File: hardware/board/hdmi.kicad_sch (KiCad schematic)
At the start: 1 part, among them U1 RK3568

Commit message: emmc stuff
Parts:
- U1: LCSC (none) -> C3345225
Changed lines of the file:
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@@
+			)
+		)
+		(property "LCSC" "C3345225"
+			(at 27.94 78.74 0)
+			(effects
+				(font
+					(size 1.27 1.27)
+				)
+				(hide yes)
 			)
 		)

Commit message: start of ethernet
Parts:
- added C147: 1uF X5R 10V, Capacitor_SMD:C_0402_1005Metric, symbol Device:C
- added D12, D13: ESD5344D, lcsc:DFN2510-10_L2.5-W1.0-P0.50-BL, symbol lcsc:ESD5344D
- added D14, D15: B5819WS_C916992, lcsc:SOD-323_L1.7-W1.3-LS2.5-RD, symbol lcsc:B5819WS_C916992
- added J1: HDMI_A, Connector_Video:HDMI_A_Amphenol_10029449-x01xLF_Horizontal, symbol Connector:HDMI_A
- added Q6, Q7, Q8: 2SK3018_C194460, lcsc:SOT-323-3_L2.0-W1.3-P1.30-LS2.1-BR, symbol lcsc:2SK3018_C194460
- added R82, R85: 1.8K 5%, Resistor_SMD:R_0402_1005Metric, symbol Device:R
- added R83, R84: 10K 5%, Resistor_SMD:R_0402_1005Metric, symbol Device:R
- added R86: 27K 5%, Resistor_SMD:R_0402_1005Metric, symbol Device:R
- added R87: 1K 5%, Resistor_SMD:R_0402_1005Metric, symbol Device:R
- added R88: 100K 5%, Resistor_SMD:R_0402_1005Metric, symbol Device:R
- added unit 13 of U1
- added U28, U29, U30, U31: ESD5341N, lcsc:DFN1006-2L-RD, symbol lcsc:ESD5341N
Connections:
- new net: D13.1, J1.12 (CK-)
- new net: D13.2, J1.10 (CK+)
- new net: D13.4, J1.9 (D0-)
- new net: D13.5, J1.7 (D0+)
- new net: D12.1, J1.1 (D2+)
- new net: D12.2, J1.3 (D2-)
- new net: D12.4, J1.4 (D1+)
- new net: D12.5, J1.6 (D1-)
- new net: Q7.1 (G), R85.2
- new net: D15.1 (K), R82.1, R85.1
- new net: Q6.1 (G), R82.2
- new net GND: C147.2, D12.3, D12.8, D13.3, D13.8, J1.11 (CKS), J1.17 (GND), J1.2 (D2S), J1.5 (D1S), J1.8 (D0S), J1.SH, R88.2, U28.2, U29.2, U30.2, U31.2
- new net HDMITX_CEC_M0: Q8.2 (S), R86.2
- new net HDMITX_SCL: Q6.2 (S), R83.2
- new net HDMITX_SDA: Q7.2 (S), R84.2
- new net HDMI_TX0N_PORT: D13.7
- new net HDMI_TX0P_PORT: D13.6
- new net HDMI_TX1N_PORT: D12.6
- new net HDMI_TX1P_PORT: D12.7
- new net HDMI_TX2N_PORT: D12.9
- new net HDMI_TX2P_PORT: D12.10
- new net HDMI_TXCLKN_PORT: D13.10
- new net HDMI_TXCLKP_PORT: D13.9
- new net HDMI_TXDDC_SCL_PORT: J1.15 (SCL), Q6.3 (D), U30.1
- new net HDMI_TXDDC_SDA_PORT: J1.16 (SDA), Q7.3 (D), U29.1
- new net HDMI_TX_CEC_PORT: J1.13 (CEC), Q8.3 (D), U31.1
- new net HDMI_TX_HPDIN: R87.1
- new net HDMI_TX_HPD_PORT: J1.19 (HPD), R87.2, R88.1, U28.1
- new net VCC_3V3: R83.1, R84.1, R86.1
- new net VCC_5V0: D14.2 (A), D15.2 (A), Q8.1 (G)
- new net VCC_5V0_HDMI_TX: C147.1, D14.1 (K), J1.18 (+5V)
- no-connect marks 0 -> 1
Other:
- moved on the sheet: U1P

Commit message: finished schematic!
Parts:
- added C352, C364, C365, C367: 100nF X5R 10V, Capacitor_SMD:C_0201_0603Metric, symbol Device:C
- added C366, C368: 4.7uF X5R 6.3V, Capacitor_SMD:C_0402_1005Metric, symbol Device:C
- added L12: L_Iron_Coupled_Small, lcsc:FILTER-SMD_4P-L2.0-W1.2-BL_DLW21H, symbol Device:L_Iron_Coupled_Small
- added R209, R210, R211, R212, R213, R214, R215, R216: 2.2R 5%, Resistor_SMD:R_0402_1005Metric, symbol Device:R
- added R217: 1.62K 1%, Resistor_SMD:R_0201_0603Metric, symbol Device:R
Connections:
- net GND: now also C352.2, C364.2, C365.2, C366.2, C367.2, C368.2, R217.1
- net HDMITX_CEC_M0: now also U1.AH6 (GPIO4_D1_U)
- net HDMITX_SCL: now also U1.AG8 (GPIO4_C7_U)
- net HDMITX_SDA: now also U1.AG7 (GPIO4_D0_U)
- net HDMI_TX0N_PORT: now also R210.1
- net HDMI_TX0P_PORT: now also R209.1
- net HDMI_TX1N_PORT: now also R212.1
- net HDMI_TX1P_PORT: now also R211.1
- net HDMI_TX2N_PORT: now also R214.1
- net HDMI_TX2P_PORT: now also R213.1
- net HDMI_TXCLKN_PORT: now also L12.3, R216.1
- net HDMI_TXCLKP_PORT: now also L12.1, R215.1
- net HDMI_TX_AVDD_0V9: now also C365.1, C366.1
- net HDMI_TX_HPDIN: now also U1.AB18 (HDMI_TX_HPDIN), C364.1
- net VCC_3V3: now also U1.V12 (VCCIO7), C352.1
- net PCIE30X2_WAKEn_M2: now reaches U1.AA11 (GPIO4_C3_D)
- net TYPEC_SW_SEL_GPIO4_D2: now reaches U1.AB9 (GPIO4_D2_D)
- net PCIE30X2_CLKREQn_M2: now reaches U1.AF8 (GPIO4_C2_D)
- net PCIE30X2_PERSTn_M2: now reaches U1.AH7 (GPIO4_C4_D)
- net at U1.AA18 (HDMI_TX_REXT): now also R217.2
- net at U1.AG19 (HDMI_TX_CLKN): now also L12.4, R216.2
- net at U1.AG20 (HDMI_TX_D0P): now also R209.2
- net at U1.AG21 (HDMI_TX_D1P): now also R211.2
- net at U1.AG22 (HDMI_TX_D2P): now also R213.2
- net at U1.AH19 (HDMI_TX_CLKP): now also L12.2, R215.2
- net at U1.AH20 (HDMI_TX_D0N): now also R210.2
- net at U1.AH21 (HDMI_TX_D1N): now also R212.2
- net at U1.AH22 (HDMI_TX_D2N): now also R214.2
- net VCCA1V8_IMAGE: now reaches U1.W18 (HDMI_TX_AVDD_1V8)
- net VCCA1V8_IMAGE: now also C367.1, C368.1
- no-connect marks 1 -> 3
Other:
- note added: "Diff 100 Ohm ±10%"
- note added: "HDMI"
- moved on the sheet: C147, D12, D13, D15, J1, Q6, Q7, R82, R83, R84, R85, U1M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

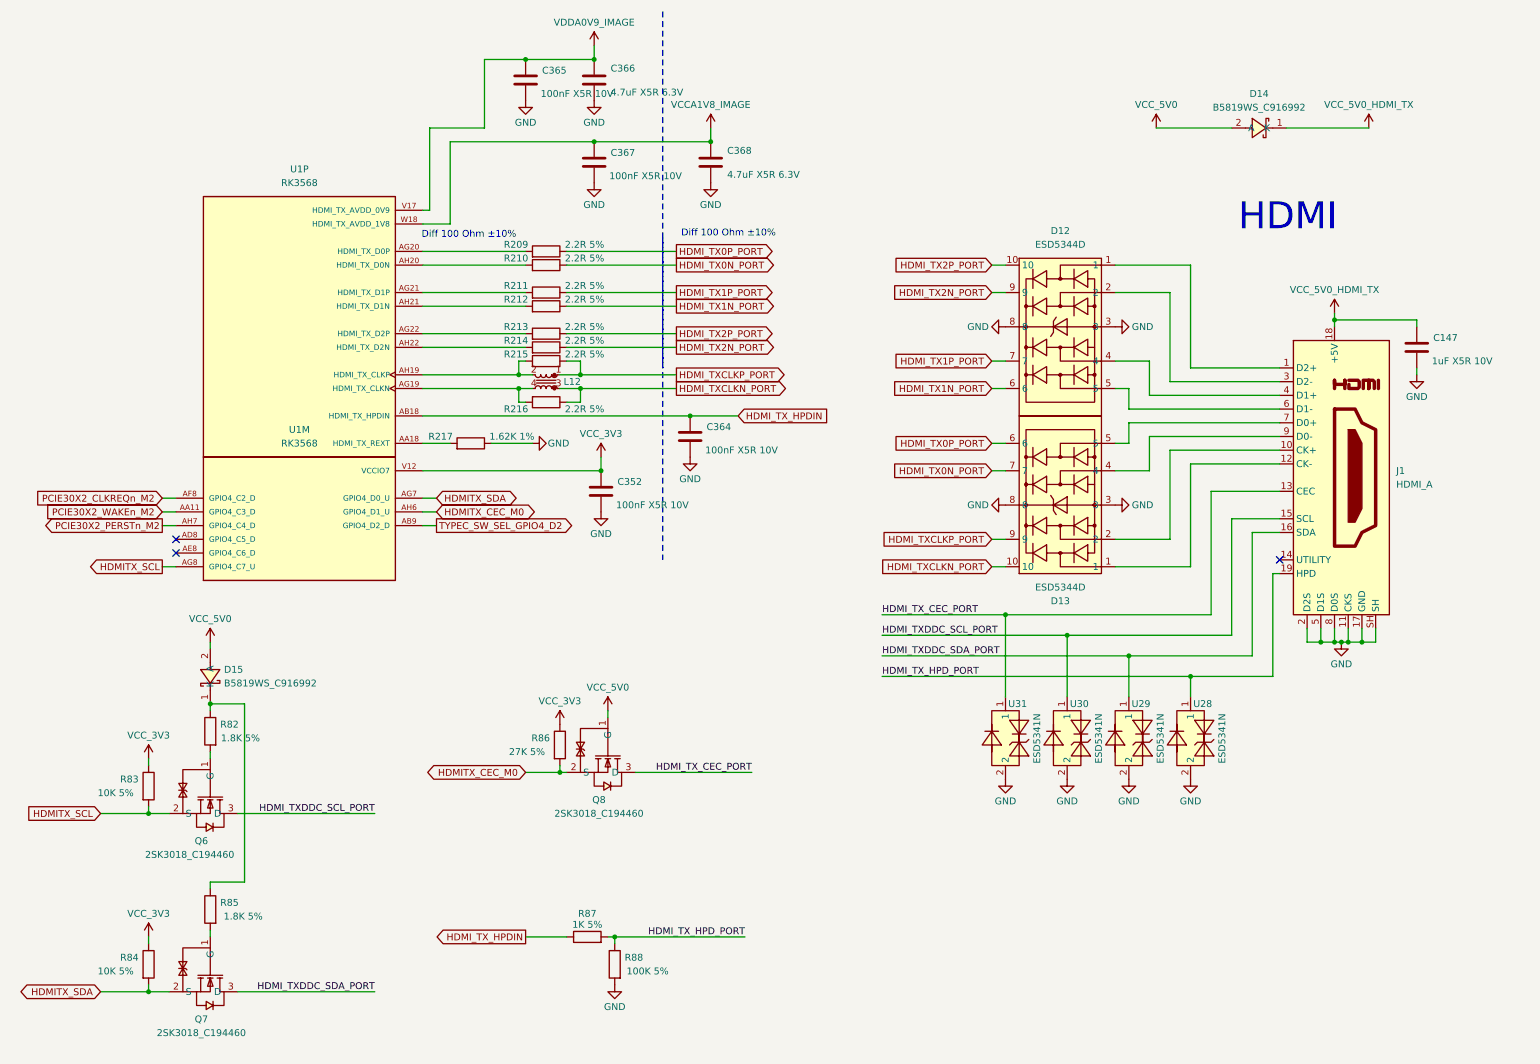
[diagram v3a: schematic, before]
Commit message: finished beautifying schematic
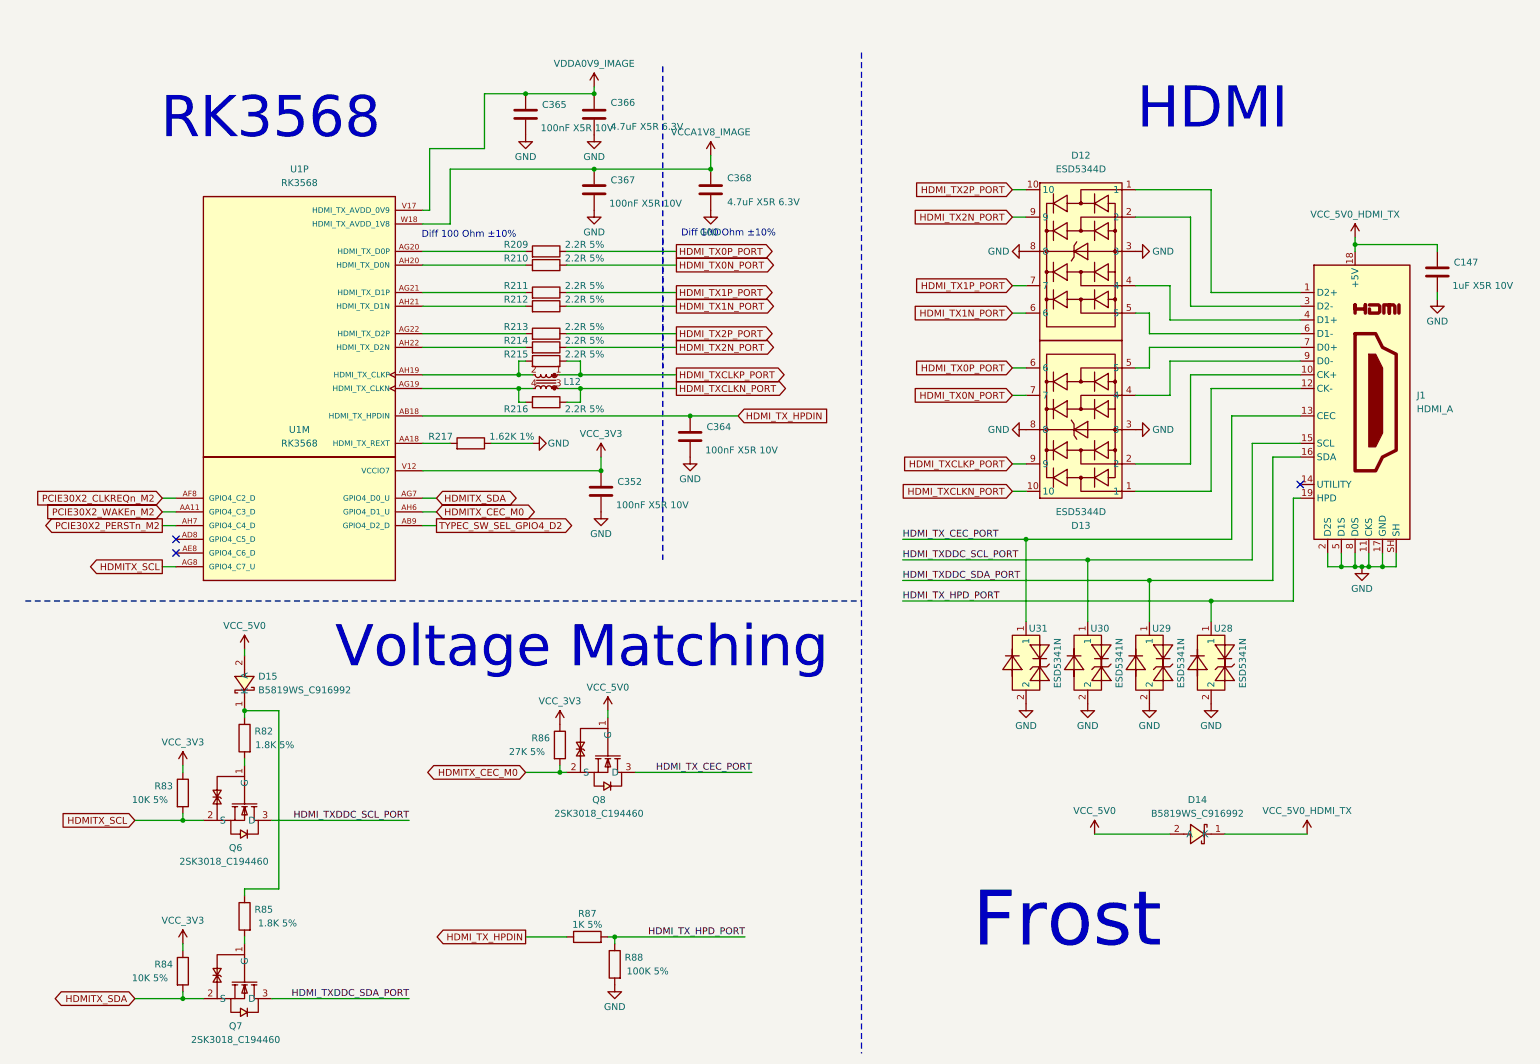
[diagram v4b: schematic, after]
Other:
- note added: "Frost"
- note added: "RK3568"
- note added: "Voltage Matching"
- moved on the sheet: C147, C365, C366, C367, C368, D12, D13, D14, D15, J1, Q6, Q7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
